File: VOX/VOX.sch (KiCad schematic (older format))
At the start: 12 parts, among them Q1 BC548, Q2 BC548, T1 TRANSFO-AUDIO

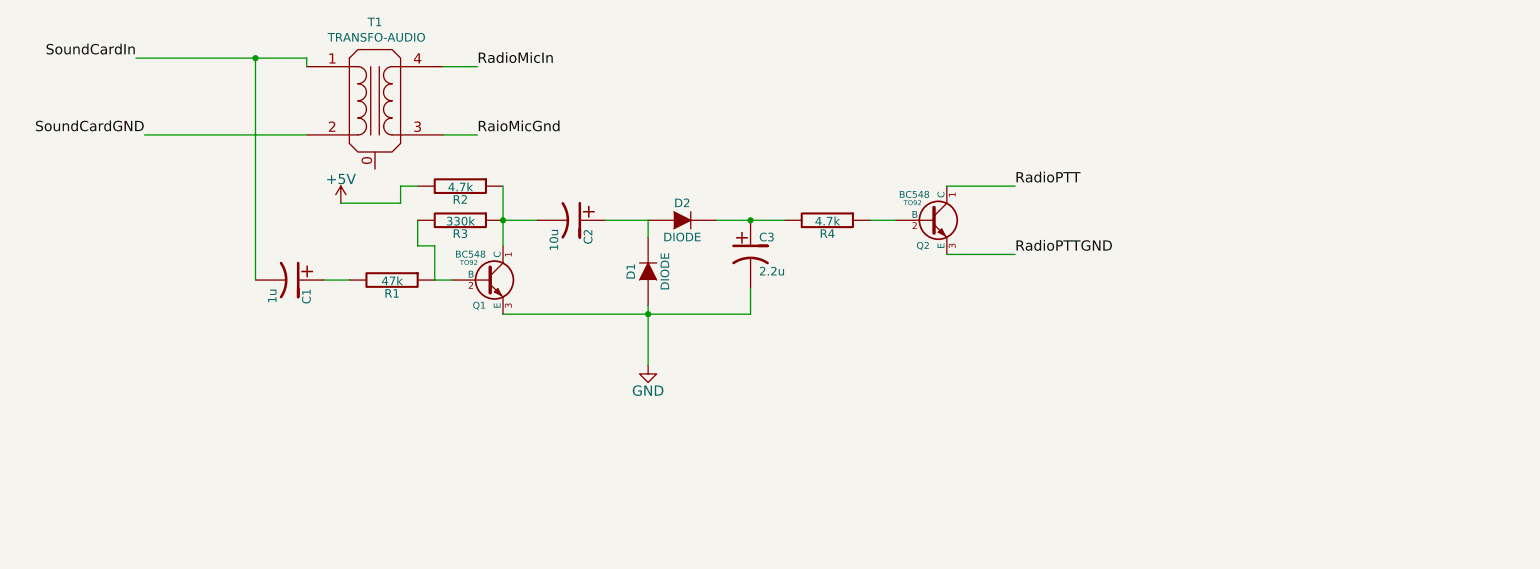
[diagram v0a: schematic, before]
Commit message: update to VOX
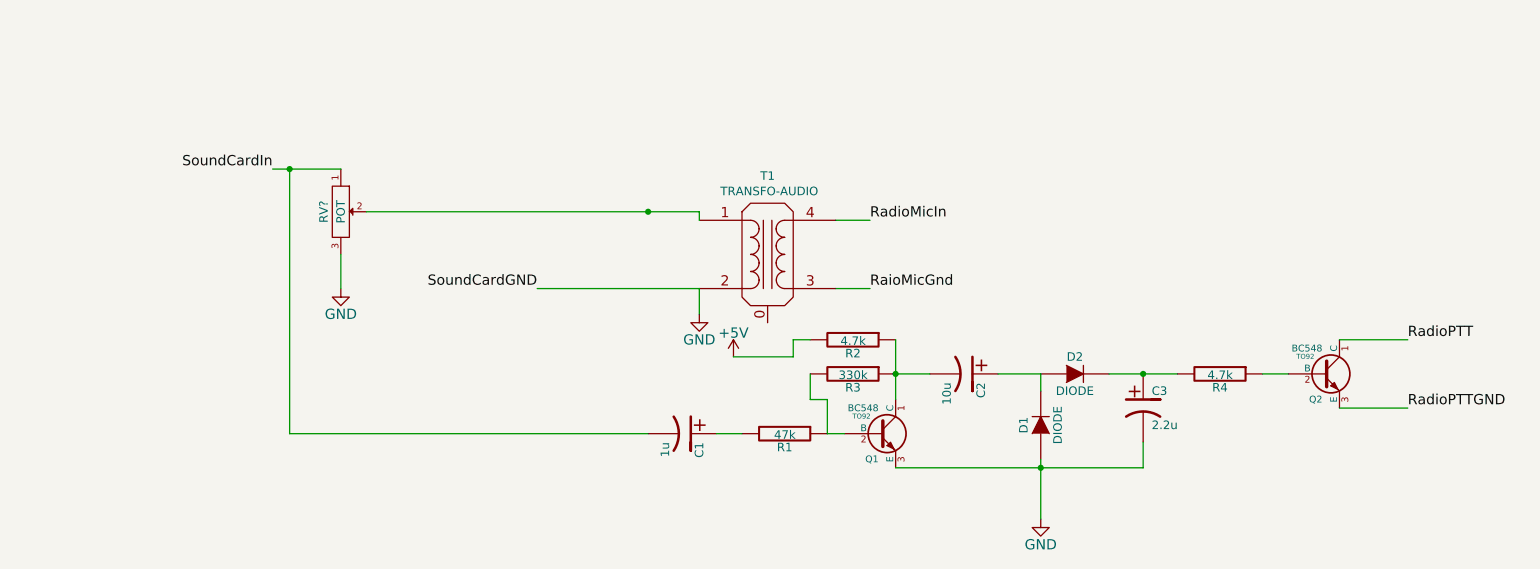
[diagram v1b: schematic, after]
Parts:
- added RV?: POT, symbol POT
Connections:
- net SoundCardGND is gone; now on net GND: T1.2 (AB)
- net GND: now also RV?.3
- net SoundCardIn: now also RV?.1; no longer T1.1 (AA)
- new net: RV?.2, T1.1 (AA)
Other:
- moved on the sheet: C1, C2, C3, D1, D2, Q1, Q2, R1, R2, R3, R4, T1

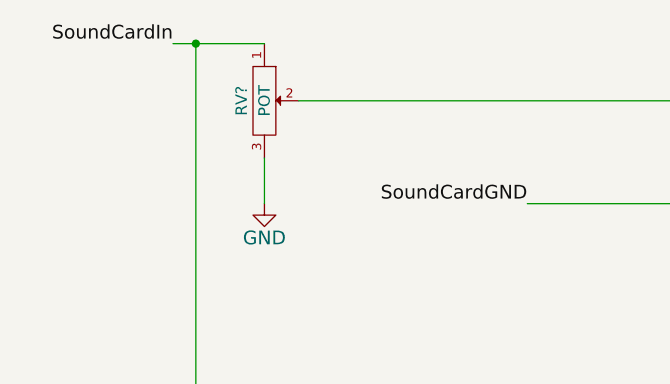
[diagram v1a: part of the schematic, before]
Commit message: values for pot
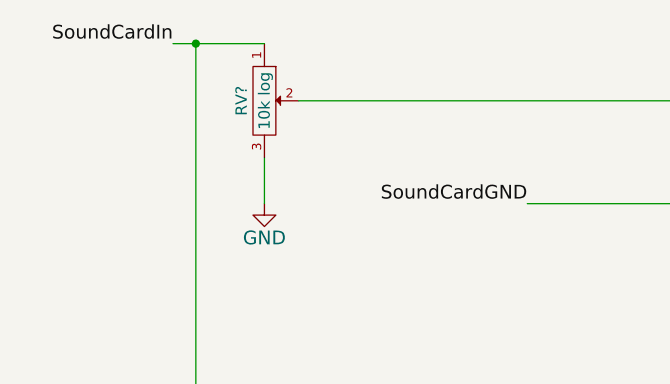
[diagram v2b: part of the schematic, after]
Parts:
- RV?: value POT -> 10k log
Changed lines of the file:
@@
 LIBS:contrib
 LIBS:valves
+LIBS:VOX-cache
 EELAYER 25 0
 EELAYER END
@@
 P 2350 3000
 F 0 "RV?" H 2350 2900 50  0000 C CNN
-F 1 "POT" H 2350 3000 50  0000 C CNN
+F 1 "10k log" H 2350 3000 50  0000 C CNN
 F 2 "" H 2350 3000 60  0000 C CNN
 F 3 "" H 2350 3000 60  0000 C CNN
